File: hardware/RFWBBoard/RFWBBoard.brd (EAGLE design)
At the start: 90 x 56 mm, 89 parts, among them IC1 24LC025ST, J1 CON-71742-3003-BOT, M1 MOUNT-HOLE3.3, M2 MOUNT-HOLE3.3, M3 MOUNT-HOLE3.3, M4 MOUNT-HOLE3.3, U1 MAX2830IPC-7351, U2 LDB212G4010C-001, U3 LDB212G4010C-001, U4 AD8132MSOP8, U5 AD8132MSOP8, U6 AD8132MSOP8, U7 AD8132MSOP8, X1 LTI-SASF54GT, X2 LTI-SASF54GT, X4 LTI-SASF54GT, X5 LTI-SASF54GT, X6 LTI-SASF54GT, X7 LTI-SASF54GT

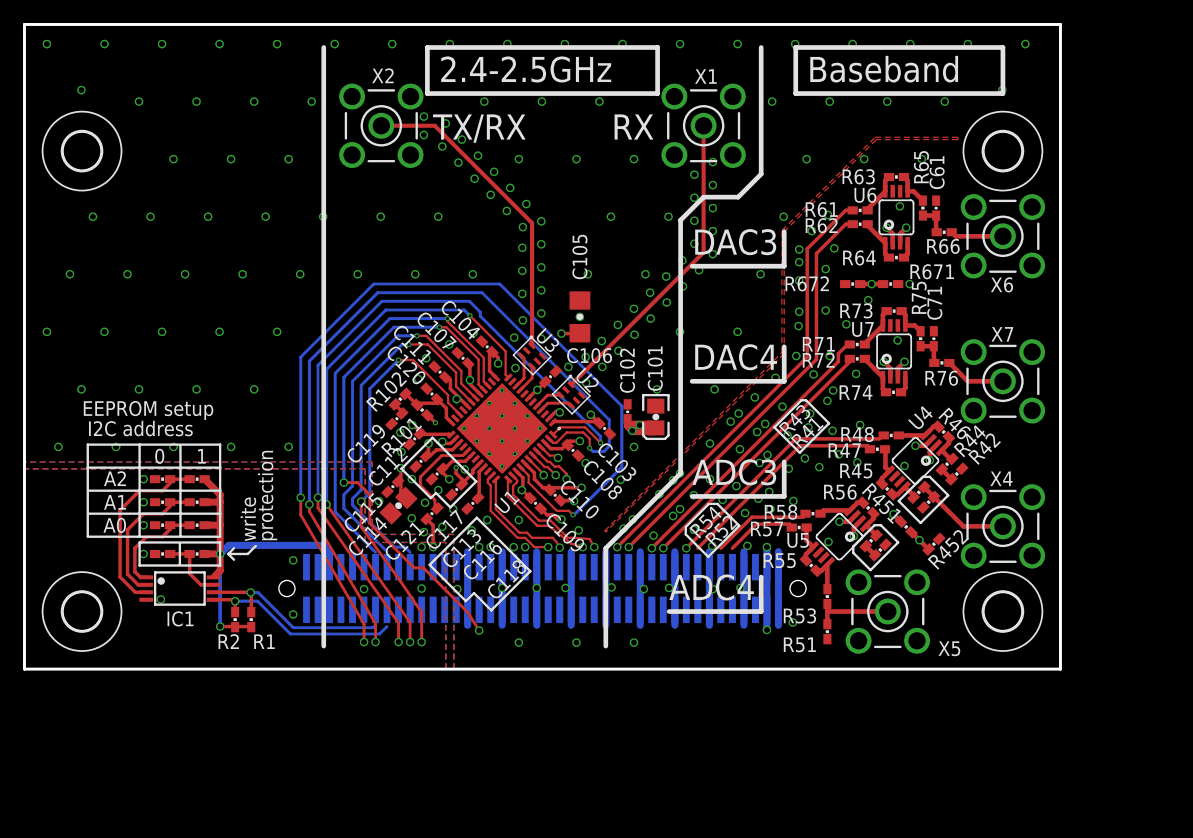
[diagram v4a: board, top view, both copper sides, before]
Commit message: - Layout update - Oscillator added
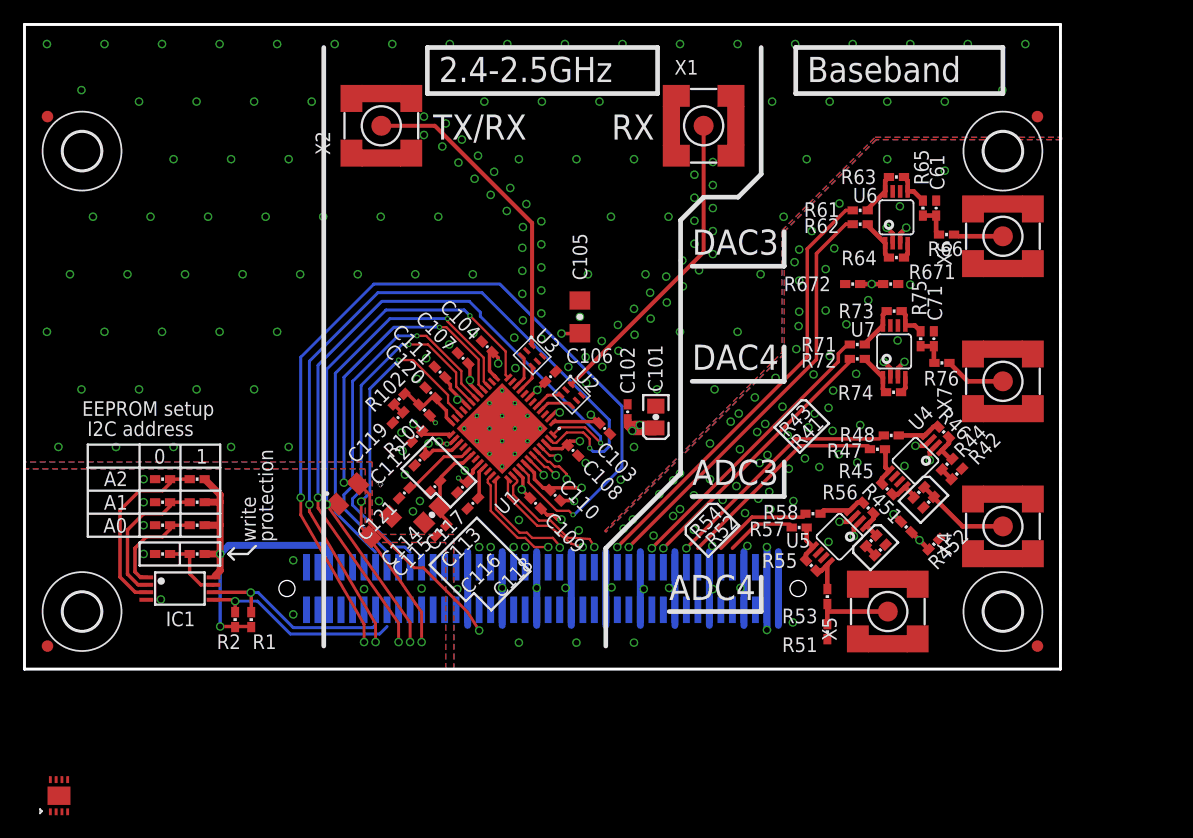
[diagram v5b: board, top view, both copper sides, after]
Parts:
- added M5, M6, M7, M8: FIDUCIAL1X2, RFWBBoard:FIDUCIAL-1X2
- added U8: LMV112, RFWBBoard:LLP-8
- added X3: FOX924B, RFWBBoard:FOX924
- X1, X2, X4, X5, X6, X7: value LTI-SASF54GT -> SMA-SMD; device RFWBBoard:LTI-SASF54GT -> RFWBBoard:SMA-SMD
- moved C115 5.66 mm to (36.2, 12.1)
- moved C114 3.01 mm to (35.4, 13.4)
- moved C121 3.00 mm to (33.0, 15.3)
- moved C116 1.12 mm to (35.6, 15.8)
- moved C118 0.54 mm to (38.0, 15.8)
- moved C112 0.28 mm to (34.1, 20.2)
- moved R66 0.28 mm to (80.1, 37.8)
- moved R101 0.20 mm to (34.8, 22.5)
- moved C119 0.14 mm to (32.5, 21.9)
- moved C120 0.14 mm to (35.3, 24.0)
- moved C113 0.14 mm to (34.4, 18.1)
- moved R102 0.10 mm to (32.5, 23.4)
- turned X2 to 90 degrees
- turned X4 to 90 degrees
- turned X5 to 90 degrees
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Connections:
- net ADC1+ renamed RXBBQ+
- net ADC1- renamed RXBBQ-
- net ADC2+ renamed RXBBI+
- net ADC2- renamed RXBBI-
- net DAC1+ renamed TXBBQ+
- net DAC1- renamed TXBBQ-
- net DAC2+ renamed TXBBI+
- net DAC2- renamed TXBBI-
- removed net SPI1_MISO: J1.22
- new net GND: U8.5
- new net N$36: C121.2, X3.3
- new net VCC: U8.1
- net A3V3: now also X3.4
- net AGND: now also X1.2@1, X1.2@2, X1.2@3, X1.2@4, X1.2@5, X1.2@6, X2.2@1, X2.2@2, X2.2@3, X2.2@4, X2.2@5, X2.2@6, X3.2, X4.2@1, X4.2@2, X4.2@3, X4.2@4, X4.2@5, X4.2@6, X5.2@1, X5.2@2, X5.2@3, X5.2@4, X5.2@5, X5.2@6, X6.2@1, X6.2@2, X6.2@3, X6.2@4, X6.2@5, X6.2@6, X7.2@1, X7.2@2, X7.2@3, X7.2@4, X7.2@5, X7.2@6; no longer X1.2, X1.3, X1.4, X1.5, X2.2, X2.3, X2.4, X2.5, X4.2, X4.3, X4.4, X4.5, X5.2, X5.3, X5.4, X5.5, X6.2, X6.3, X6.4, X6.5, X7.2, X7.3, X7.4, X7.5
- net CLK1: no longer C121.2
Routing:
- net A3V3: track 192.7 -> 181.8 mm, vias 23 -> 21
- net CLK1: track 2.67 -> 0.00 mm, vias 1 -> 0
- net N$6: track 8.15 -> 5.86 mm
- net N$10: track 5.35 -> 4.23 mm
- net N$29: track 4.59 -> 3.80 mm
- net N$9: track 27.2 -> 26.7 mm
- net AGND: vias 249 -> 244
- added copper zone on layer 15, net A3V3
- added copper zone on layer 14, net AGND
- added copper zone on layer 15, net AGND
- added copper zone on layer 14, net DGND
- added copper zone on layer 15, net DGND
- added copper zone on layer 14, net N$35
- added copper zone on layer 15, net N$35
- added copper zone on layer 16, net N$35
- added copper zone on layer 2, net N$35
- added copper zone on layer 3, net N$35
- removed copper zone on layer 2, net A3V3

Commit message: - Layout update
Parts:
- added C122: 1000pF, RFWBBoard:C0402
- added C123, C126, C129: 10uF, RFWBBoard:C0805
- added C124, C127, C130: 100nF, RFWBBoard:C0402
- added C125, C128, C131: 100pF, RFWBBoard:C0402
- added U9: ICS85320I, RFWBBoard:SOIC8
- U8: value LMV112 -> ICS83021I; device RFWBBoard:LLP-8 -> RFWBBoard:SOIC8
- moved LOGO3 55.9 mm to (47.5, 60.5)
- moved LOGO1 37.8 mm to (32.5, 61.0)
- moved U8 34.7 mm to (24.5, 16.3)
- moved LOGO2 20.8 mm to (17.5, 60.5)
- moved X3 11.2 mm to (29.7, 25.0), turned to 270 degrees
- moved C106 6.82 mm to (49.6, 31.0), turned to 270 degrees
- moved R1 4.52 mm to (17.8, 8.40), turned to 90 degrees
- moved C101 3.01 mm to (54.0, 19.0)
- moved C102 3.01 mm to (52.2, 19.4)
- moved C121 2.82 mm to (34.1, 17.9), turned to 180 degrees
- moved C118 2.62 mm to (39.3, 18.1)
- moved C109 2.52 mm to (45.8, 16.5)
- moved C110 2.51 mm to (47.3, 17.3)
- moved C117 2.48 mm to (40.1, 16.6)
- moved U1 2.39 mm to (42.8, 22.9)
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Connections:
- removed net GND: U8.5
- removed net VCC: U8.1
- new net N$37: J1.11
- new net N$38: J1.13
- new net N$39: C122.1, U9.7
- new net N$40: J1.23
- new net N$41: J1.19
- new net N$42: J1.21
- net !SHDN: no longer J1.19
- net A3V3: now also C123.1, C124.1, C125.1, C126.1, C127.1, C128.1, C129.1, C130.1, C131.1, U8.8, U9.8
- net AGND: now also C123.2, C124.2, C125.2, C126.2, C127.2, C128.2, C129.2, C130.2, C131.2, U8.5, U9.5
- net ANTSEL: no longer J1.13
- net CLK1: now also U8.2, U9.2
- net CLK2: now also U8.3, U9.3
- net LD: no longer J1.21
- net N$36: now also C122.2, U8.7
- net RXHP: no longer J1.11
- net RXTX: no longer J1.17
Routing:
- net A3V3: track 181.8 -> 83.2 mm, vias 21 -> 27
- net RXHP: track 79.1 -> 24.1 mm
- net ANTSEL: track 68.5 -> 33.0 mm
- net RXTX: track 63.7 -> 34.1 mm
- net RSSI: track 45.4 -> 29.0 mm
- net !SHDN: track 47.6 -> 31.4 mm
- net N$36: track 0.00 -> 15.6 mm
- net I2C_SDA: track 17.5 -> 31.6 mm
- net I2C_SCL: track 17.2 -> 30.4 mm
- net CLK2: track 0.00 -> 12.1 mm, vias 0 -> 1
- net CLK1: track 0.00 -> 10.4 mm, vias 0 -> 1
- net LD: track 34.9 -> 26.0 mm
- net !CS: track 36.0 -> 28.3 mm
- net TXBBQ-: track 10.9 -> 14.4 mm
- net AGND: track 69.6 -> 66.1 mm, vias 244 -> 293
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
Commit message: - Decoupling capacitors - Layout update - Schematic update
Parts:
- added C41, C51: 10uF, RFWBBoard:CPOL2012
- added C42, C45, C52, C62, C67, C72: 100nF, RFWBBoard:C0402
- added C43, C53, C63, C73: 10nF, RFWBBoard:C0402
- added C64, C74: 100pF, RFWBBoard:C0402
- added R3, R4: DNP, RFWBBoard:R0603
- C61, C71: value 100pF -> 10uF; device RFWBBoard:C0402 -> RFWBBoard:CPOL2012
- RA00, RA01, RA10, RA11, RA20, RA21, RWP0, RWP1: value NONE -> DNP
- moved C61 25.0 mm to (96.5, 22.0), turned to 0 degrees
- moved C71 22.5 mm to (96.5, 14.5), turned to 0 degrees
- moved C101 2.12 mm to (55.5, 20.5)
- moved C102 2.12 mm to (53.7, 20.9)
- moved C123 1.60 mm to (27.9, 30.1)
- moved C124 1.50 mm to (29.5, 29.6)
- moved C125 1.50 mm to (30.5, 29.6)
- moved R452 0.87 mm to (78.2, 10.4), turned to 135 degrees
- moved R672 0.45 mm to (71.9, 33.0)
- moved R451 0.18 mm to (76.5, 12.5)
- moved C126 0.10 mm to (23.9, 23.0)
- moved C129 0.10 mm to (18.7, 23.0)
- moved R671 0.07 mm to (75.2, 33.4)
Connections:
- removed net N$37: J1.11
- removed net N$38: J1.13
- removed net N$40: J1.23
- removed net N$41: J1.19
- removed net N$42: J1.21
- net !SHDN: now also J1.13
- net A3V3: now also C41.+, C42.1, C43.1, C51.+, C52.1, C53.1, C61.+, C62.1, C63.1, C71.+, C72.1, C73.1
- net AGND: now also C41.-, C42.2, C43.2, C45.2, C51.-, C52.2, C53.2, C61.-, C62.2, C63.2, C64.2, C67.2, C71.-, C72.2, C73.2, C74.2, R3.2, R4.2; no longer C61.2, C71.2
- net ANTSEL: now also J1.19
- net DGND: now also R3.1, R4.1
- net LD: now also J1.11
- net N$27: now also C64.1; no longer C61.1
- net N$33: now also C74.1; no longer C71.1
- net RXHP: now also J1.17
- net RXTX: now also J1.21
- net V_BIAS_ADC: now also C45.1
- net V_BIAS_DAC: now also C67.1
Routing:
- net DGND: track 0.00 -> 20.7 mm, vias 23 -> 26
- net V_BIAS_DAC: track 17.7 -> 19.8 mm
- net RXTX: track 34.1 -> 35.8 mm
- net LD: track 26.0 -> 27.7 mm
- net ANTSEL: track 33.0 -> 34.4 mm
- net A3V3: track 83.2 -> 82.2 mm
- net RXHP: track 24.1 -> 25.2 mm
- net !CS: track 28.3 -> 29.1 mm
- net V_BIAS_ADC: track 17.9 -> 18.6 mm
- net N$9: track 25.2 -> 24.6 mm
- net I2C_SDA: track 31.6 -> 31.0 mm
- net I2C_SCL: track 30.4 -> 29.8 mm
- net !SHDN: track 31.4 -> 32.0 mm
- net AGND: vias 293 -> 334
- added copper zone on layer 1, net N$43
- added copper zone on layer 14, net N$43
- added copper zone on layer 15, net N$43
- added copper zone on layer 16, net N$43
- added copper zone on layer 2, net N$43
- added copper zone on layer 3, net N$43

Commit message: - Layout update
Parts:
- moved C61 26.4 mm to (70.1, 21.5), turned to 90 degrees
- moved C62 24.6 mm to (71.9, 21.1), turned to 90 degrees
- moved C63 23.7 mm to (72.9, 21.1), turned to 90 degrees
- moved C45 22.3 mm to (96.5, 26.1)
- moved R451 22.3 mm to (93.5, 27.0)
- moved R452 22.3 mm to (95.2, 24.9)
- moved C51 22.0 mm to (80.0, 19.7)
- moved C52 20.4 mm to (79.4, 21.6)
- moved C72 20.3 mm to (93.0, 32.5)
- moved C73 20.3 mm to (93.0, 31.5)
- moved C53 19.6 mm to (79.4, 22.6)
- moved C71 18.0 mm to (96.0, 32.5), turned to 90 degrees
- moved C41 16.3 mm to (80.0, 32.3)
- moved C42 14.7 mm to (79.4, 34.2)
- moved C43 14.7 mm to (79.4, 35.2)
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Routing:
- net A3V3: track 82.2 -> 94.6 mm, vias 27 -> 33
- net ADC3-: track 22.4 -> 19.1 mm
- net ADC3+: track 20.1 -> 17.6 mm
- net V_BIAS_ADC: track 18.6 -> 16.8 mm
- net N$18: track 3.34 -> 1.65 mm
- net N$20: track 3.35 -> 5.03 mm
- net N$19: track 4.09 -> 5.64 mm
- net ADC4-: track 9.97 -> 8.69 mm
- net N$13: track 3.76 -> 2.65 mm
- net N$23: track 3.67 -> 2.57 mm
- net N$28: track 3.69 -> 2.62 mm
- net N$24: track 3.67 -> 2.70 mm
- net N$30: track 3.67 -> 2.72 mm
- net N$21: track 2.61 -> 1.75 mm
- net N$27: track 2.90 -> 2.05 mm
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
